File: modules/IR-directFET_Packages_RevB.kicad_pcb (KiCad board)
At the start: 2 copper layers, 15 parts

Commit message: some 3d models for IR direct fet added
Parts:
- moved T 13.8 mm to (80.2, 41.2)
- moved T 4.81 mm to (85.8, 104.8)
- moved T 1.58 mm to (237.5, 43.5)

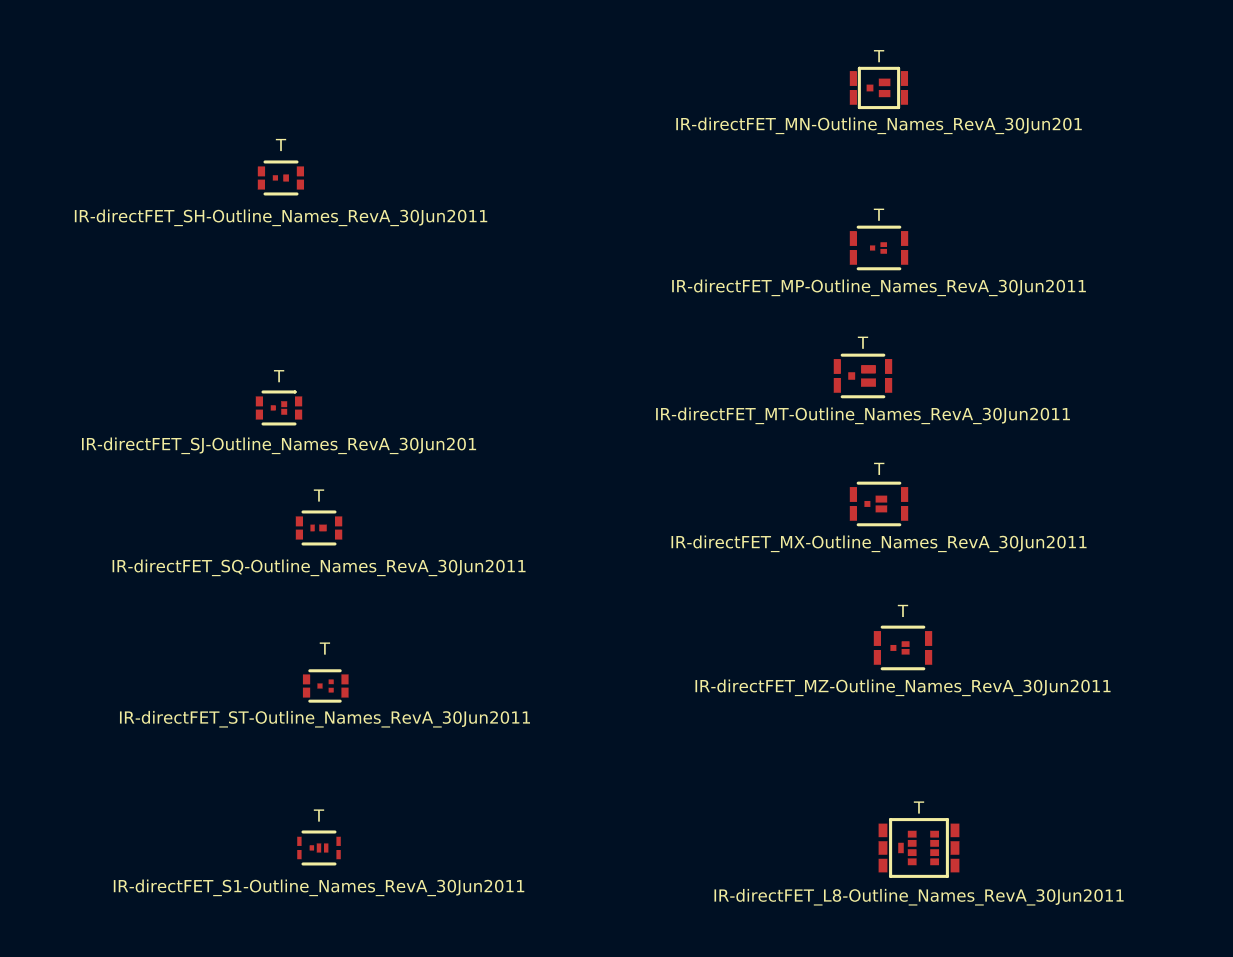
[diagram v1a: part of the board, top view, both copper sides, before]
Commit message: some IRF direct FET mesh models added
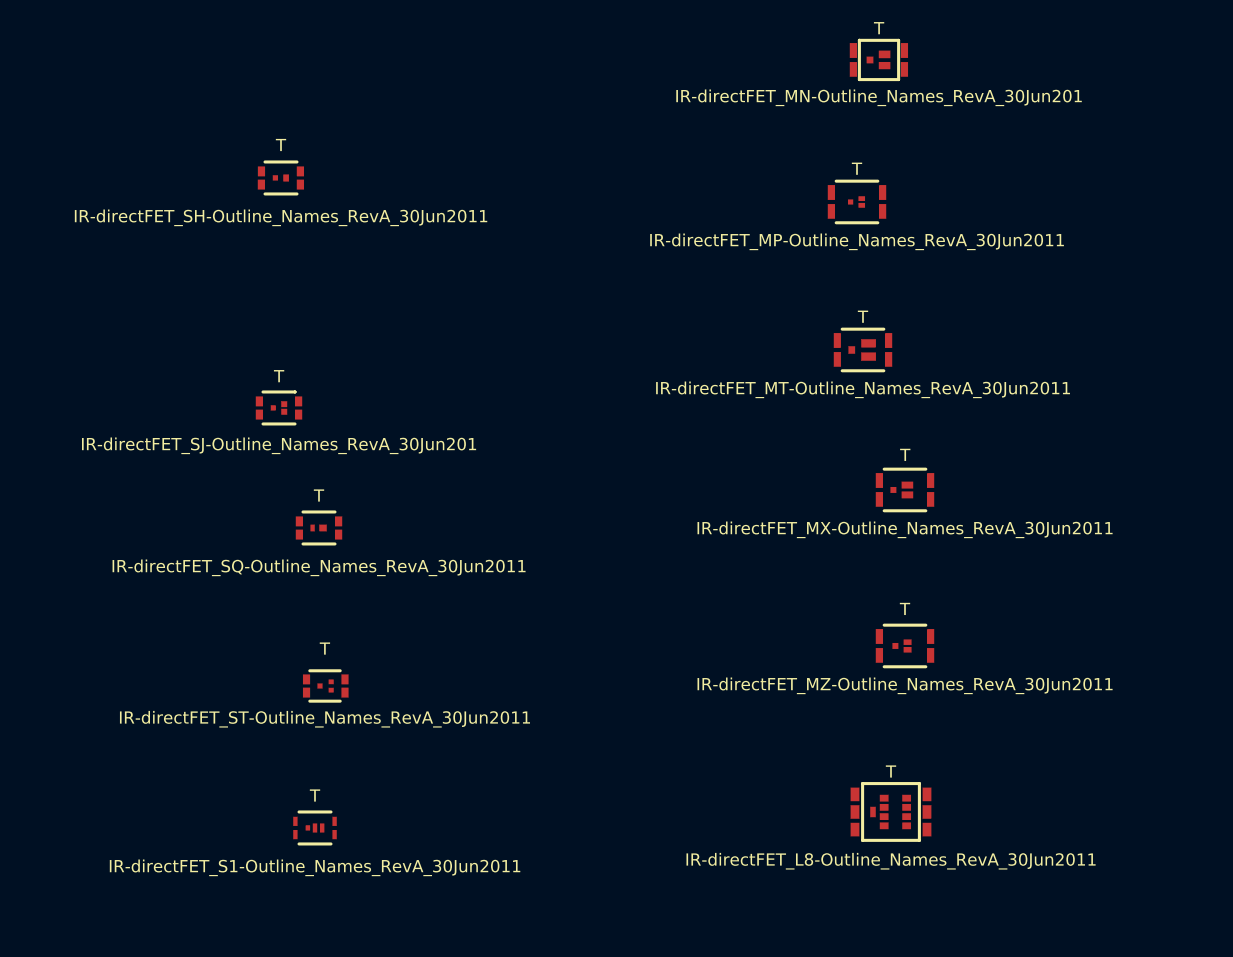
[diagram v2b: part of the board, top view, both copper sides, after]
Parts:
- moved T 6.37 mm to (152.2, 44.2)
- moved T 5.70 mm to (156.5, 120.5)
- moved T 3.69 mm to (158.2, 80.2)
- moved T 3.50 mm to (155.0, 26.5)
- moved T 3.25 mm to (153.0, 62.8)
- moved T 2.55 mm to (84.5, 122.5)
- moved T 0.35 mm to (158.2, 99.8)
